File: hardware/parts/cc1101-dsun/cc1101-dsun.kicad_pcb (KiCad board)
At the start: 2 copper layers, 15 x 30 mm, 4 parts, among them J1 Conn_02x04_Odd_Even, J2 Conn_Coaxial

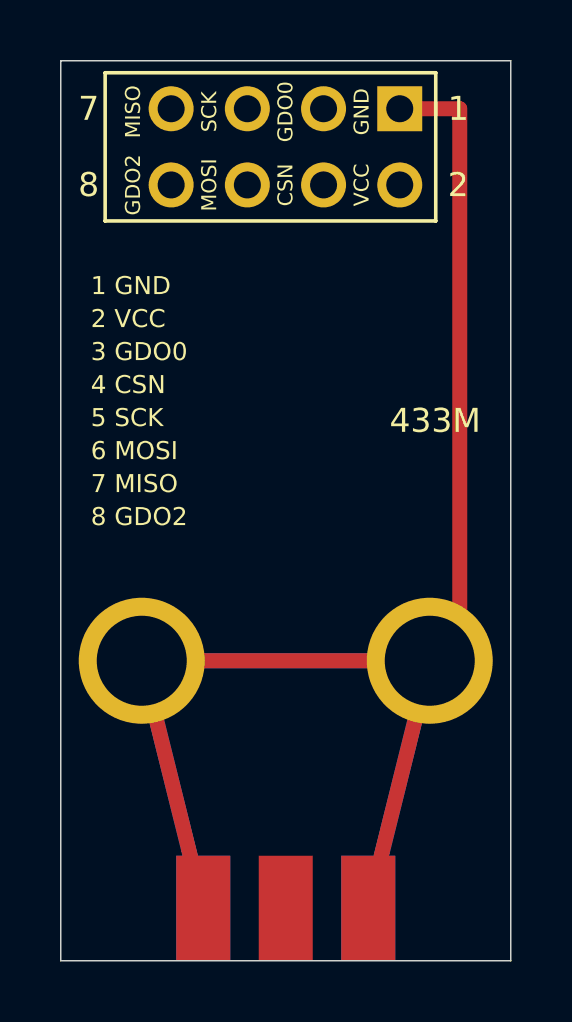
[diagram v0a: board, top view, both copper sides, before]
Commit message: Add the green D-Sun CC1101 board with the same assets as the blue E07-M1101D
The user's second CC1101 board ("433MHz D-Sun CC1101", green; EasyEDA calls
it RF1101SE V3.1) carries the same eight signals on the same 2x4 header,
with the GND/VCC column in the same place but the three signal columns
permuted, so it does not fit the socket adapter's pinout and is supported
with jumper wires instead.

* scripts/generate_dsun.py -> hardware/parts/cc1101-dsun: outline 14.4 x
  30, header rows 2.1 / 4.6 from the edge, columns 2.9..10.5 from the left
  long edge, two 1.8 mm holes beside the SMA jack, pin names on both sides
  and the original's back-side legend grid.  Dimensions measured from the
  user's photos with the E07-M1101D as the scale (+/- 0.3 mm).
* 3D models (cc1101-dsun.step, -components.step) attached to the board.
* Pinout diagram: third column, green, with the back legend; wiring diagram
  docs/images/wiring-cc1101-dsun.svg (its wires cannot all nest; the chip
  select runs along the back of the board below the header).
* README: comparison table with the blue board, why the socket does not
  take it, a component-board section, 3D model row; CI regenerates it and
  the manufacturing notes cover it.

The photos also showed both boards' edge-mount SMA jacks have their ground
legs 5.5 mm apart, not 8.5: the shared SMA footprint, the E07 reference
board, the SX1278 adapter's SMA ground routing (now skirting the antenna
wire hole) and the 3D jack model follow.

Strap change for the jumper-wire builds: the SuperMini has one G pin (the
brown wire's), so the Ra-02's strap wire goes from GPIO5 to GPIO4, which
firmware drives low while reading the strap; documented with the read
procedure.

Co-Authored-By: Claude Fable 5.1 <noreply@anthropic.com>
Claude-Session: https://claude.ai/code/session_01JoGdh4Cg3VtTTDZi4gQuiN
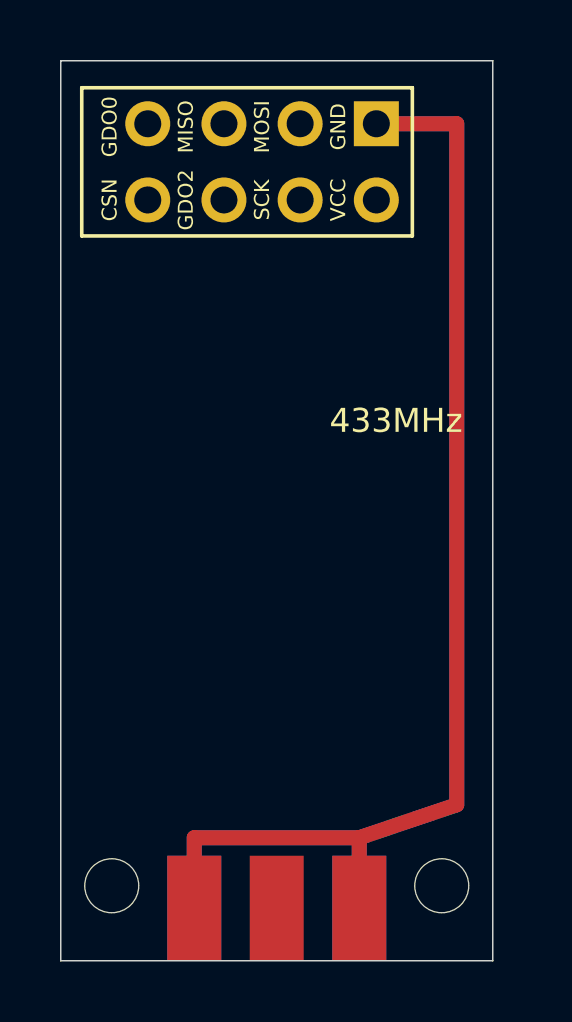
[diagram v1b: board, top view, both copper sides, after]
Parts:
- H1, H2: value MountingHole_Pad -> MountingHole; footprint E07:MountingHole_3.0mm_Pad_4.2mm -> DSun:MountingHole_1.8mm
- J1: footprint E07:PinHeader_2x04_P2.54mm_E07 -> DSun:PinHeader_2x04_P2.54mm_DSun
- J2: footprint E07:SMA_EdgeMount_E07 -> DSun:SMA_EdgeMount_E07
- moved H1 7.57 mm to (101.7, 127.5)
- moved H2 7.51 mm to (112.7, 127.5)
- moved J1 0.93 mm to (110.5, 102.1)
- moved J2 0.30 mm to (107.2, 130.0)
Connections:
- H1 pad 1: GND -> (no net)
- H2 pad 1: GND -> (no net)
- J1 pad 3: GDO0 -> MOSI
- J1 pad 4: CSN -> SCK
- J1 pad 5: SCK -> MISO
- J1 pad 6: MOSI -> GDO2
- J1 pad 7: MISO -> GDO0
- J1 pad 8: GDO2 -> CSN
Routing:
- net GND: track 74.6 -> 78.0 mm
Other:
- board size 15 x 30 mm -> 14.4 x 30 mm
- board text added: "433MHz"
- board text added: "433MHz D-Sun CC1101"
- board text added: "D-Sun CC1101 form factor"
- board text removed: "1"
- board text removed: "1 GND"
- board text removed: "2"
- board text removed: "2 VCC"
- board text removed: "3 GDO0"
- board text removed: "4 CSN"
- board text removed: "433M"
- board text removed: "5 SCK"
- board text removed: "6 MOSI"
- board text removed: "7"
- board text removed: "7 MISO"
- board text removed: "8"
- board text removed: "8 GDO2"
- board text removed: "E07-M1101D form factor"
